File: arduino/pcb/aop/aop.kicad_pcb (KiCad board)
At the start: 2 copper layers, 45 x 55 mm, 22 parts, among them Q1 AO4435, SW1 SW_Push, SW2 SW_Push, U1 ESP32-C3_SUPERMINI_TH, U2 DS3231M

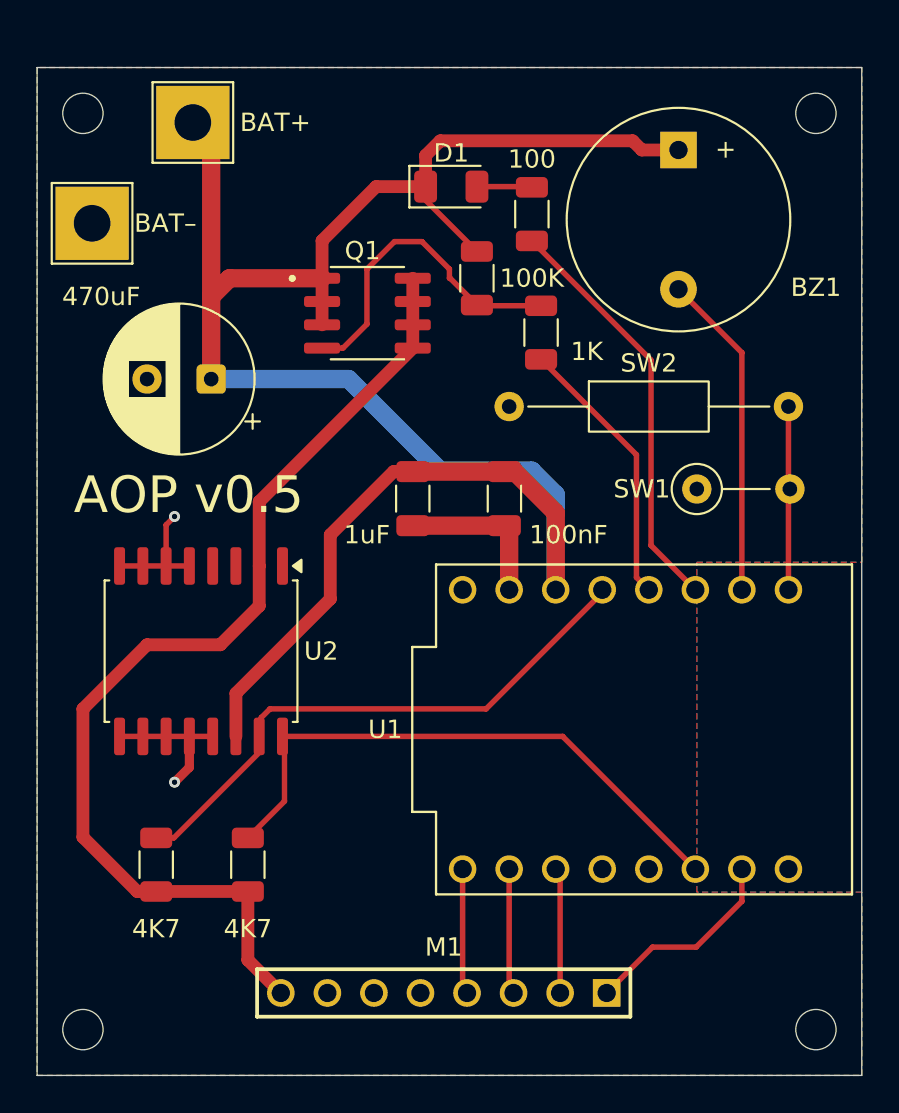
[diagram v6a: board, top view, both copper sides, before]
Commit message: [pcb] Rearrange pins, combine buzzer and led to free UART
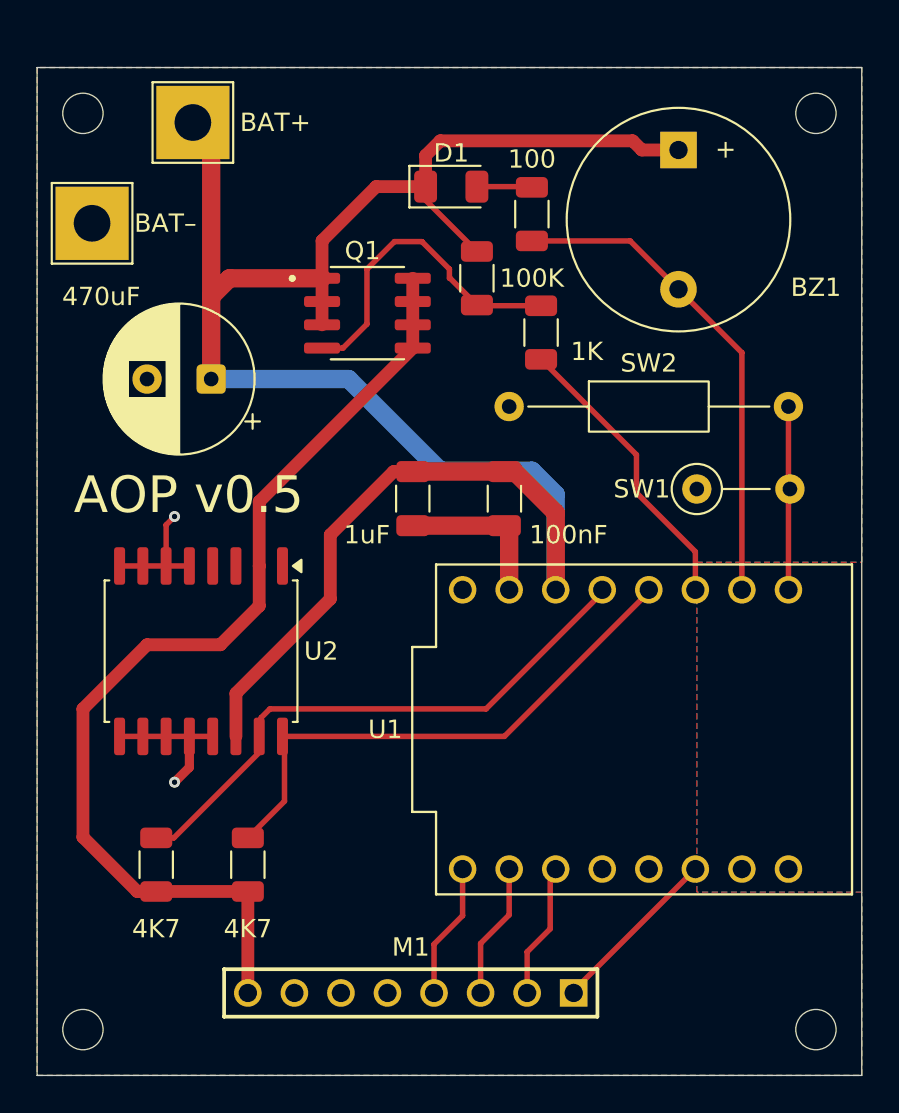
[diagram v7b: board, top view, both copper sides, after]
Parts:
- moved M1 1.80 mm to (146.4, 131.0)
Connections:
- R2 pad 2: Net-(U1-GPIO3) -> Net-(U1-GPIO2)
- R3 pad 1: Net-(U1-GPIO2) -> Net-(BZ1--)
- R5 pad 2: Net-(U1-GPIO10) -> Net-(U1-GPIO3)
- U1 pad 10: Net-(U1-GPIO10) -> Net-(M1-SDA)
- U1 pad 20: Net-(M1-SDA) -> unconnected-(U1-GPIO20-Pad20)
- U2 pad 16: Net-(U1-GPIO10) -> Net-(U1-GPIO3)
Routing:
- net Net-(U1-GPIO10): track 31.8 -> 0.00 mm
- net Net-(U1-GPIO3): track 15.0 -> 29.6 mm
- net Net-(BZ1--): track 17.8 -> 26.9 mm
- net Net-(U1-GPIO2): track 22.7 -> 16.1 mm
- net Net-(M1-SDA): track 11.2 -> 9.51 mm
- net +3.3VA: track 56.8 -> 56.1 mm
- net Net-(M1-MISO): track 6.86 -> 7.41 mm
- net Net-(M1-MOSI): track 6.86 -> 7.41 mm
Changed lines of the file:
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@@
 		(capping no)
 		(filling no)
-		(zone_defaults)
 		(pcbplotparams
 			(layerselection 0x00000000_00000000_55555555_5755f5ff)
@@
 	(footprint "RFID-RC522:RFID-RC522_1"
 		(layer "F.Cu")
-		(at 148.19 131 180)
+		(at 146.39 131 180)
 		(descr "MFRC522 RFID Module<br><br>Created by: Wai Weng")
 		(property "Reference" "M1"
@@
 			(layers "F.Cu" "F.Mask" "F.Paste")
 			(roundrect_rratio 0.222222)
-			(net "Net-(U1-GPIO3)")
+			(net "Net-(U1-GPIO2)")
 			(pintype "passive")
 		)
@@
 			(layers "F.Cu" "F.Mask" "F.Paste")
 			(roundrect_rratio 0.222222)
-			(net "Net-(U1-GPIO2)")
+			(net "Net-(BZ1--)")
 			(pintype "passive")
 		)
@@
 			(layers "F.Cu" "F.Mask" "F.Paste")
 			(roundrect_rratio 0.25)
-			(net "Net-(U1-GPIO10)")
+			(net "Net-(U1-GPIO3)")
 			(pinfunction "SCL_16")
 			(pintype "input")
@@
 			(layers "*.Cu" "*.Mask")
 			(remove_unused_layers no)
-			(net "Net-(U1-GPIO10)")
+			(net "Net-(M1-SDA)")
 			(pinfunction "GPIO10_10")
 			(pintype "bidirectional")
@@
 			(layers "*.Cu" "*.Mask")
 			(remove_unused_layers no)
-			(net "Net-(M1-SDA)")
+			(net "unconnected-(U1-GPIO20-Pad20)")
 			(pinfunction "GPIO20_20")
 			(pintype "bidirectional")
@@
 			(layers "F.Cu" "F.Mask" "F.Paste")
 			(roundrect_rratio 0.222222)
-			(net "Net-(U1-GPIO10)")
+			(net "Net-(U1-GPIO3)")
 			(pintype "passive")
 		)
@@
 	)
 	(segment
-		(start 159.58 128.5)
-		(end 161.96 128.5)
+		(start 155.28 130.88)
+		(end 155.28 131)
 		(width 0.3)
 		(layer "F.Cu")
@@
 	)
 	(segment
-		(start 157.08 131)
-		(end 159.58 128.5)
+		(start 161.92 124.24)
+		(end 155.28 130.88)
 		(width 0.3)
 		(layer "F.Cu")
@@
 	)
 	(segment
-		(start 161.96 128.5)
-		(end 164.46 126)
+		(start 154 124.54)
+		(end 154 127.5)
 		(width 0.3)
 		(layer "F.Cu")
-		(net "Net-(M1-SDA)")
+		(net "Net-(M1-SCK)")
 	)
 	(segment
-		(start 164.46 126)
-		(end 164.46 124.24)
+		(start 154 127.5)
+		(end 152.74 128.76)
 		(width 0.3)
 		(layer "F.Cu")
-		(net "Net-(M1-SDA)")
+		(net "Net-(M1-SCK)")
 	)
 	(segment
-		(start 154.54 124.48)
-		(end 154.3 124.24)
+		(start 152.74 128.76)
+		(end 152.74 131)
 		(width 0.3)
 		(layer "F.Cu")
@@
 	)
 	(segment
-		(start 154.54 131)
-		(end 154.54 124.48)
+		(start 151.76 124.24)
+		(end 151.76 126.74)
 		(width 0.3)
 		(layer "F.Cu")
-		(net "Net-(M1-SCK)")
+		(net "Net-(M1-MOSI)")
 	)
 	(segment
-		(start 151.76 130.76)
-		(end 152 131)
+		(start 151.76 126.74)
+		(end 150.2 128.3)
 		(width 0.3)
 		(layer "F.Cu")
@@
 	)
 	(segment
-		(start 151.76 124.24)
-		(end 151.76 130.76)
+		(start 150.2 128.3)
+		(end 150.2 131)
 		(width 0.3)
 		(layer "F.Cu")
@@
 	)
 	(segment
-		(start 149.22 130.76)
-		(end 149.46 131)
+		(start 147.66 128.34)
+		(end 147.66 131)
+		(width 0.3)
+		(layer "F.Cu")
+		(net "Net-(M1-MISO)")
+	)
+	(segment
+		(start 149.22 126.78)
+		(end 147.66 128.34)
 		(width 0.3)
 		(layer "F.Cu")
@@
 	(segment
 		(start 149.22 124.24)
-		(end 149.22 130.76)
+		(end 149.22 126.78)
 		(width 0.3)
 		(layer "F.Cu")
@@
 	)
 	(segment
-		(start 137.5 129.2)
-		(end 139.3 131)
+		(start 137.5 125.4625)
+		(end 137.5 131)
 		(width 0.7)
 		(layer "F.Cu")
@@
 	)
 	(segment
-		(start 137.5 125.4625)
-		(end 137.5 129.2)
-		(width 0.7)
-		(layer "F.Cu")
-		(net "+3.3VA")
-	)
-	(segment
 		(start 148.5 92)
 		(end 148.5375 92)
@@
 	)
 	(segment
-		(start 159.38 109)
-		(end 158.706001 108.326001)
+		(start 137.5 122.5375)
+		(end 139.5 120.5375)
 		(width 0.3)
 		(layer "F.Cu")
@@
 	)
 	(segment
-		(start 158.706001 108.326001)
-		(end 158.706001 101.631001)
+		(start 139.5 120.5375)
+		(end 139.5 117)
 		(width 0.3)
 		(layer "F.Cu")
@@
 	)
 	(segment
-		(start 158.706001 101.631001)
-		(end 153.5 96.425)
+		(start 151.5 117)
+		(end 159.38 109.12)
+		(width 0.3)
+		(layer "F.Cu")
+		(net "Net-(U1-GPIO3)")
+	)
+	(segment
+		(start 159.38 109.12)
+		(end 159.38 109)
+		(width 0.3)
+		(layer "F.Cu")
+		(net "Net-(U1-GPIO3)")
+	)
+	(segment
+		(start 139.5 117)
+		(end 151.5 117)
 		(width 0.3)
 		(layer "F.Cu")
@@
 	)
 	(segment
-		(start 164.46 96.06)
-		(end 161 92.6)
+		(start 153 89.9625)
+		(end 158.3625 89.9625)
 		(width 0.3)
 		(layer "F.Cu")
@@
 	)
 	(segment
-		(start 164.46 109)
-		(end 164.46 96.06)
+		(start 164.46 96.06)
+		(end 161 92.6)
 		(width 0.3)
 		(layer "F.Cu")
@@
 	)
 	(segment
-		(start 159.5 106.58)
-		(end 159.5 96.4625)
-		(width 0.3)
-		(layer "F.Cu")
-		(net "Net-(U1-GPIO2)")
-	)
-	(segment
-		(start 161.92 109)
-		(end 159.5 106.58)
+		(start 164.46 109)
+		(end 164.46 96.06)
 		(width 0.3)
 		(layer "F.Cu")
-		(net "Net-(U1-GPIO2)")
+		(net "Net-(BZ1--)")
 	)
 	(segment
-		(start 159.5 96.4625)
-		(end 153 89.9625)
+		(start 158.3625 89.9625)
+		(end 161 92.6)
 		(width 0.3)
 		(layer "F.Cu")
-		(net "Net-(U1-GPIO2)")
+		(net "Net-(BZ1--)")
 	)
 	(segment
-		(start 152.5 87)
-		(end 150 87)
+		(start 156.84 109.16)
+		(end 156.84 109)
 		(width 0.3)
 		(layer "F.Cu")
-		(net "Net-(D1-A)")
+		(net "Net-(U1-GPIO4)")
 	)
 	(segment
-		(start 161.92 124.24)
-		(end 154.68 117)
+		(start 133.4625 122.5375)
+		(end 138.23 117.77)
 		(width 0.3)
 		(layer "F.Cu")
-		(net "Net-(U1-GPIO10)")
+		(net "Net-(U1-GPIO4)")
 	)
 	(segment
-		(start 139.5 117)
-		(end 139.5 120.5375)
+		(start 150.5 115.5)
+		(end 156.84 109.16)
 		(width 0.3)
 		(layer "F.Cu")
-		(net "Net-(U1-GPIO10)")
+		(net "Net-(U1-GPIO4)")
 	)
 	(segment
-		(start 154.68 117)
-		(end 139.5 117)
+		(start 138.23 117.77)
+		(end 138.23 115.975001)
 		(width 0.3)
 		(layer "F.Cu")
-		(net "Net-(U1-GPIO10)")
+		(net "Net-(U1-GPIO4)")
 	)
 	(segment
-		(start 139.5 120.5375)
-		(end 137.5 122.5375)
+		(start 132.5 122.5375)
+		(end 133.4625 122.5375)
 		(width 0.3)
 		(layer "F.Cu")
-		(net "Net-(U1-GPIO10)")
+		(net "Net-(U1-GPIO4)")
 	)
 	(segment
-		(start 156.84 109.16)
-		(end 156.84 109)
+		(start 138.705001 115.5)
+		(end 150.5 115.5)
 		(width 0.3)
 		(layer "F.Cu")
@@
 	)
 	(segment
-		(start 133.4625 122.5375)
-		(end 138.23 117.77)
+		(start 138.23 115.975001)
+		(end 138.705001 115.5)
 		(width 0.3)
 		(layer "F.Cu")
@@
 	)
 	(segment
-		(start 150.5 115.5)
-		(end 156.84 109.16)
+		(start 153.5 96.425)
+		(end 158.706001 101.631001)
 		(width 0.3)
 		(layer "F.Cu")
-		(net "Net-(U1-GPIO4)")
+		(net "Net-(U1-GPIO2)")
 	)
 	(segment
-		(start 138.23 117.77)
-		(end 138.23 115.975001)
+		(start 158.706001 103.706001)
+		(end 161.92 106.92)
 		(width 0.3)
 		(layer "F.Cu")
-		(net "Net-(U1-GPIO4)")
+		(net "Net-(U1-GPIO2)")
 	)
 	(segment
-		(start 132.5 122.5375)
-		(end 133.4625 122.5375)
+		(start 161.92 106.92)
+		(end 161.92 109)
 		(width 0.3)
 		(layer "F.Cu")
-		(net "Net-(U1-GPIO4)")
+		(net "Net-(U1-GPIO2)")
 	)
 	(segment
-		(start 138.705001 115.5)
-		(end 150.5 115.5)
+		(start 158.706001 101.631001)
+		(end 158.706001 103.706001)
 		(width 0.3)
 		(layer "F.Cu")
-		(net "Net-(U1-GPIO4)")
+		(net "Net-(U1-GPIO2)")
 	)
 	(segment
-		(start 138.23 115.975001)
-		(end 138.705001 115.5)
+		(start 152.5 87)
+		(end 150 87)
 		(width 0.3)
 		(layer "F.Cu")
-		(net "Net-(U1-GPIO4)")
+		(net "Net-(D1-A)")
 	)
 	(segment

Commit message: [pcb] Expose UART0
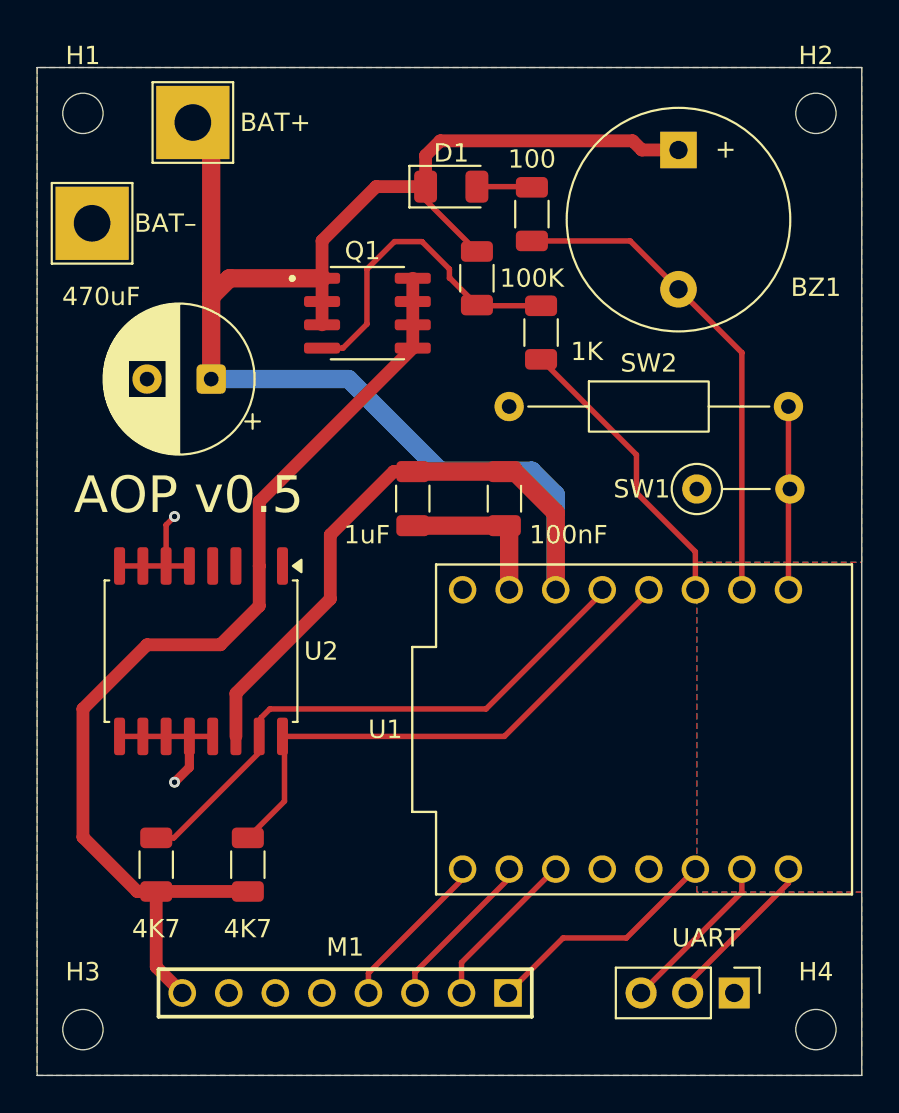
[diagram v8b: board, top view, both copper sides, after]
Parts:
- added J1: UART, Connector_PinHeader_2.54mm:PinHeader_1x03_P2.54mm_Vertical, F.Cu at (164.0, 131.0)
- moved M1 3.58 mm to (142.8, 131.0)
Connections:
- U1 pad 20: unconnected-(U1-GPIO20-Pad20) -> Net-(J1-Pin_3)
- U1 pad 21: unconnected-(U1-GPIO21-Pad21) -> Net-(J1-Pin_2)
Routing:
- net Net-(J1-Pin_3): track 0.00 -> 9.04 mm
- net Net-(J1-Pin_2): track 0.00 -> 9.04 mm
- net Net-(M1-SDA): track 9.51 -> 13.0 mm
- net Net-(M1-SCK): track 6.98 -> 8.91 mm
- net Net-(M1-MOSI): track 7.41 -> 8.89 mm
- net Net-(M1-MISO): track 7.41 -> 8.89 mm
- net +3.3VA: track 56.1 -> 56.7 mm
